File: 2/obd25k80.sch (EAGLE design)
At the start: 56 parts, among them IC1 PIC18F25K80, IC2 MCP2562, IC3 78L05, IC4 78L05, IC5 LE33CZ, J1 MA04-1, J2 DB9-M, Q1 BC547, Q2 BC557, Q3 BC547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

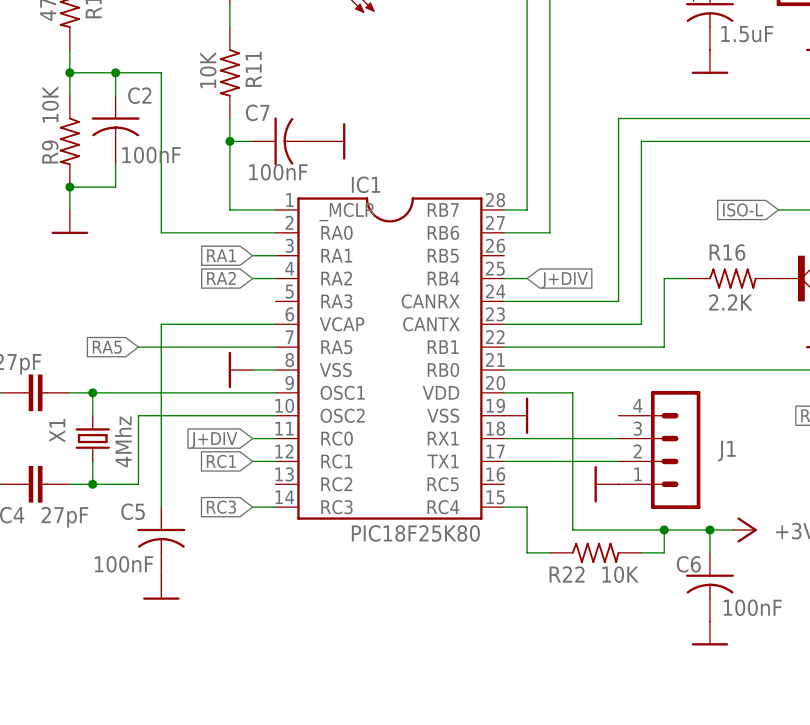
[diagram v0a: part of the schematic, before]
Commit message: Libraty updated for PIC18F25K80
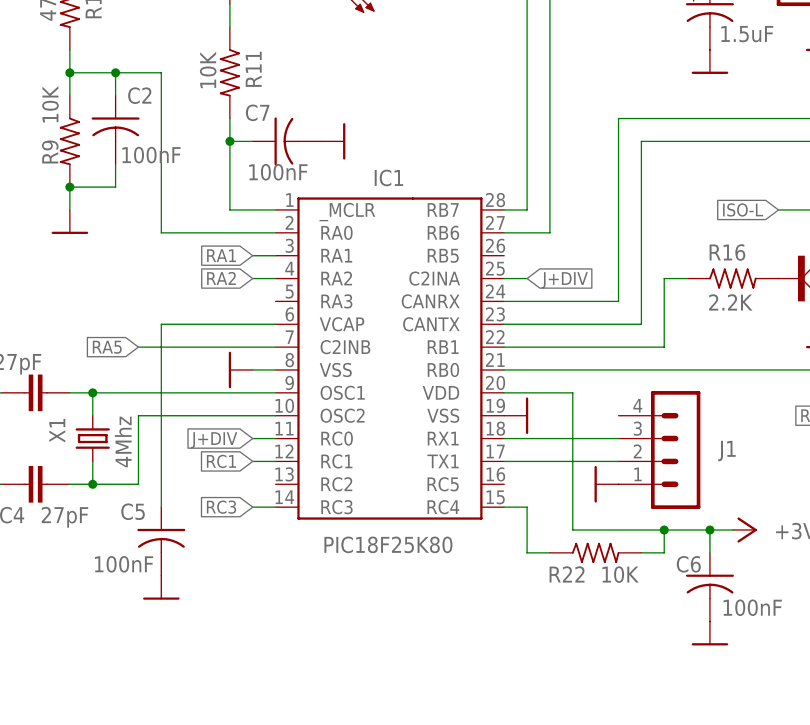
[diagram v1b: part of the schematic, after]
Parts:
- IC1: device pic18f2455:PIC18F25K80 -> pic18f2455:PIC18F25K80-2
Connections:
- net J+DIV: now also IC1.C2INA; no longer IC1.RB4
- net RA5: now also IC1.C2INB; no longer IC1.RA5
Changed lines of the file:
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@@
 <part name="GND29" library="supply1" deviceset="GND" device=""/>
 <part name="P+1" library="supply1" deviceset="+5V" device=""/>
-<part name="IC1" library="pic18f2455" deviceset="PIC18F25K80" device=""/>
+<part name="IC1" library="pic18f2455" deviceset="PIC18F25K80-2" device="" value="PIC18F25K80"/>
 <part name="+3V3" library="supply1" deviceset="+3V3" device=""/>
 <part name="R13" library="rcl" deviceset="R-US_" device="0207/10" value="330"/>
@@
 </instance>
 <instance part="IC1" gate="G$1" x="73.66" y="114.3" smashed="yes">
-<attribute name="NAME" x="69.215" y="133.985" size="1.778" layer="95"/>
-<attribute name="VALUE" x="69.215" y="95.25" size="1.778" layer="96"/>
+<attribute name="NAME" x="71.755" y="134.747" size="1.778" layer="95"/>
+<attribute name="VALUE" x="66.167" y="93.98" size="1.778" layer="96"/>
 </instance>
 <instance part="+3V3" gate="G$1" x="60.96" y="177.8" smashed="yes">
@@
 <net name="RA5" class="0">
 <segment>
-<pinref part="IC1" gate="G$1" pin="RA5"/>
+<pinref part="IC1" gate="G$1" pin="C2INB"/>
 <wire x1="60.96" y1="116.84" x2="45.72" y2="116.84" width="0.1524" layer="91"/>
 <label x="45.72" y="116.84" size="1.4224" layer="95" rot="R180" xref="yes"/>
@@
 <net name="J+DIV" class="0">
 <segment>
-<pinref part="IC1" gate="G$1" pin="RB4"/>
+<pinref part="IC1" gate="G$1" pin="C2INA"/>
 <wire x1="86.36" y1="124.46" x2="88.9" y2="124.46" width="0.1524" layer="91"/>
 <label x="88.9" y="124.46" size="1.4224" layer="95" xref="yes"/>
